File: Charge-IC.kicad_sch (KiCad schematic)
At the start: 34 parts, among them Q1 RSJ250P10, Q2 RSJ250P10, SW1 SW_DPDT_x2, SW2 SW_SPDT, U2 LTC4000-QFN

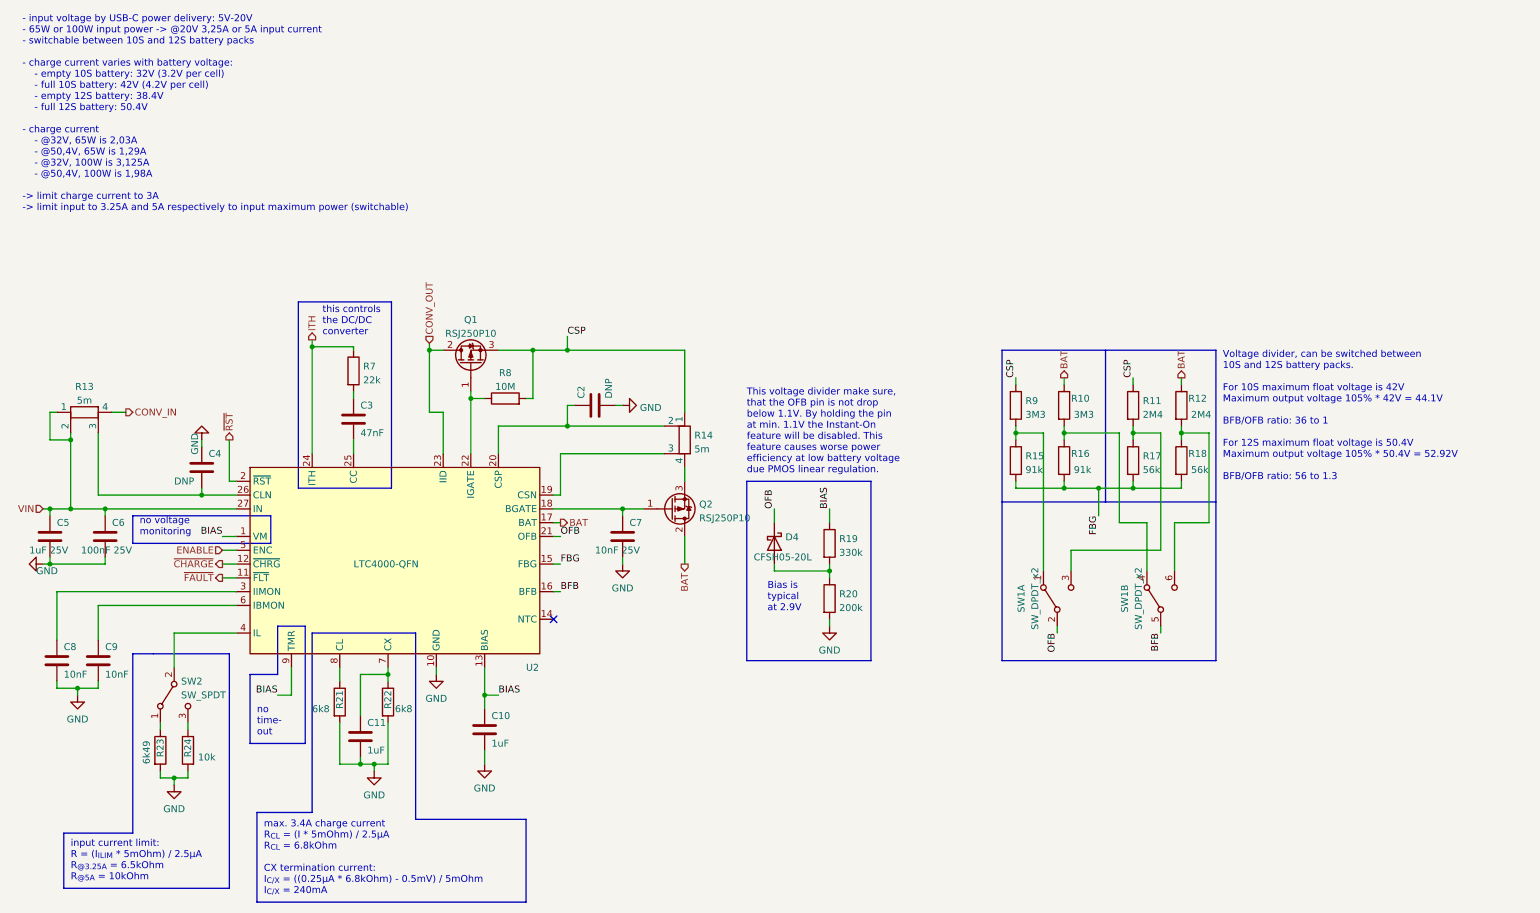
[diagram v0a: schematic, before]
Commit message: Fix wrong battery polarity Enable voltage monitoring at 15V Add caps to OFB and BFB Use another diodes Replace 1206 shunt with 0805 Replace main mosfet with bigger one Improve traces/ground planes
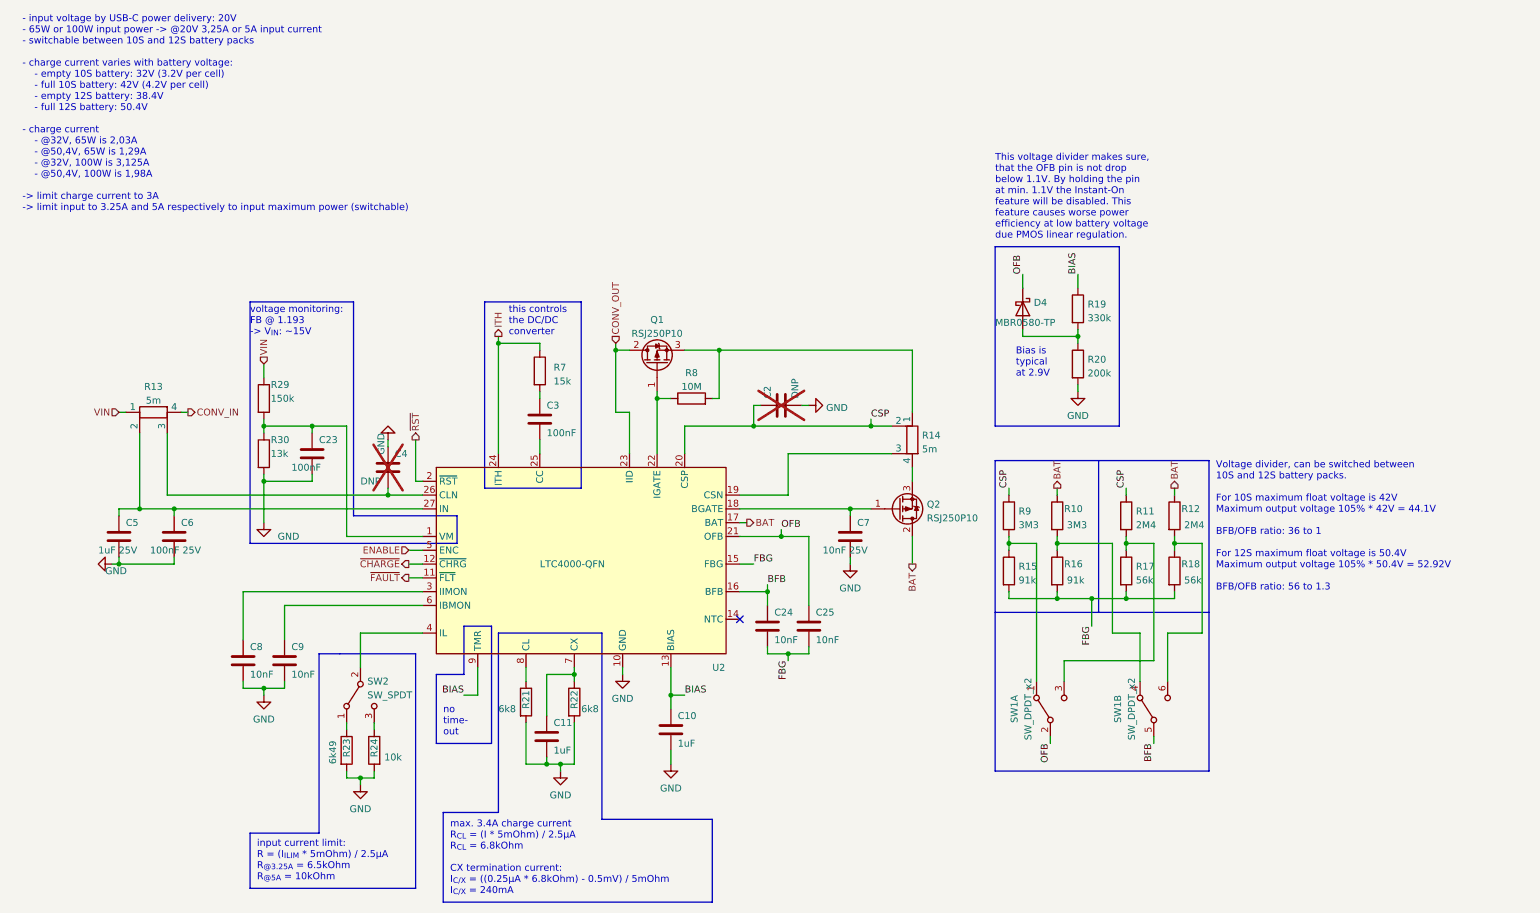
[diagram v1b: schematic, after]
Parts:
- added C23: 100nF, Capacitor_SMD:C_0603_1608Metric, symbol Device:C
- added C24, C25: 10nF, Capacitor_SMD:C_0603_1608Metric, symbol Device:C
- added R29: 150k, Resistor_SMD:R_0603_1608Metric, symbol Device:R
- added R30: 13k, Resistor_SMD:R_0603_1608Metric, symbol Device:R
- C2, C4: now not fitted
- C3: value 47nF -> 100nF
- D4: value CFSH05-20L -> MBR0580-TP; footprint extraFootprints:SOD882D -> Diode_SMD:D_SOD-123
- R13, R14: footprint extraFootprints:R_1206_3216Metric_4Kelvin -> extraFootprints:R_0805_2012Metric_4Kelvin
- R7: value 22k -> 15k
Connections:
- net BFB: now also C24.1
- net BIAS: no longer U2.1 (VM)
- net CSP: now also C2.1, R14.2, U2.20 (CSP); no longer Q1.3 (S), R14.1, R8.2
- net FBG: now also C24.2, C25.2
- net GND: now also C23.2, R30.2
- net OFB: now also C25.1
- net VIN: now also R29.1; no longer C5.1, C6.1, R13.2, U2.27 (IN)
- new net: C23.1, R29.2, R30.1, U2.1 (VM)
- new net: C5.1, C6.1, R13.2, U2.27 (IN)
- new net: Q1.3 (S), R14.1, R8.2
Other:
- note added: "- input voltage by USB-C power delivery: 20V - 65W or 100W input power -> @20V 3,25A or 5A input current - switchable between 10S and 12S battery packs - charge current varies with battery voltage: - empty 10S battery: 32V (3.2V per cell) - full 10S battery: 42V (4.2V per cell) - empty 12S battery: 38.4V - full 12S battery: 50.4V - charge current - @32V, 65W is 2,03A - @50,4V, 65W is 1,29A - @32V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"
- note added: "This voltage divider makes sure, that the OFB pin is not drop below 1.1V. By holding the pin at min. 1.1V the Instant-On feature will be disabled. This feature causes worse power efficiency at low battery voltage due PMOS linear regulation."
- note added: "voltage monitoring: FB @ 1.193 -> V_{IN}: ~15V"
- note removed: "- input voltage by USB-C power delivery: 5V-20V - 65W or 100W input power -> @20V 3,25A or 5A input current - switchable between 10S and 12S battery packs - charge current varies with battery voltage: - empty 10S battery: 32V (3.2V per cell) - full 10S battery: 42V (4.2V per cell) - empty 12S battery: 38.4V - full 12S battery: 50.4V - charge current - @32V, 65W is 2,03A - @50,4V, 65W is 1,29A - @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"
- note removed: "This voltage divider make sure, that the OFB pin is not drop below 1.1V. By holding the pin at min. 1.1V the Instant-On feature will be disabled. This feature causes worse power efficiency at low battery voltage due PMOS linear regulation."
- note removed: "no voltage monitoring"
- moved on the sheet: C10, C11, C3, C5, C6, C7, C8, C9, D4, Q1, Q2, R10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
